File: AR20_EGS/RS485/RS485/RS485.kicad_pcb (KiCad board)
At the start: 2 copper layers, 12 x 15 mm, 6 parts, among them J1 Conn_01x06_Female, J2 Conn_01x02_Female, U1 MAX3362EKA+T

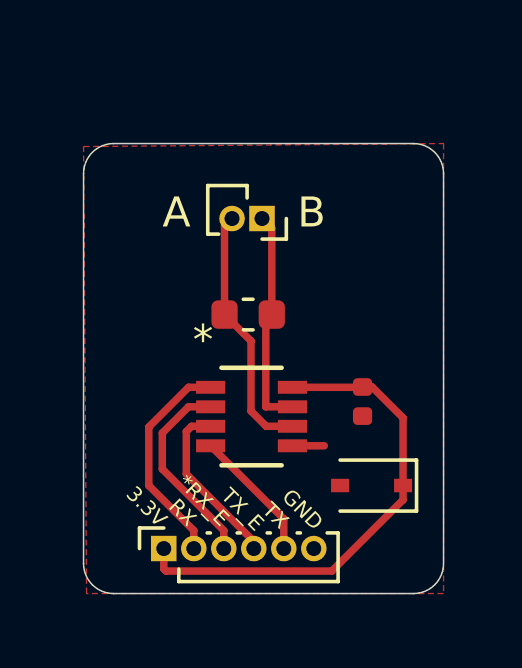
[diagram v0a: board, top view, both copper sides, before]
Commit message: Reverse polarity protection
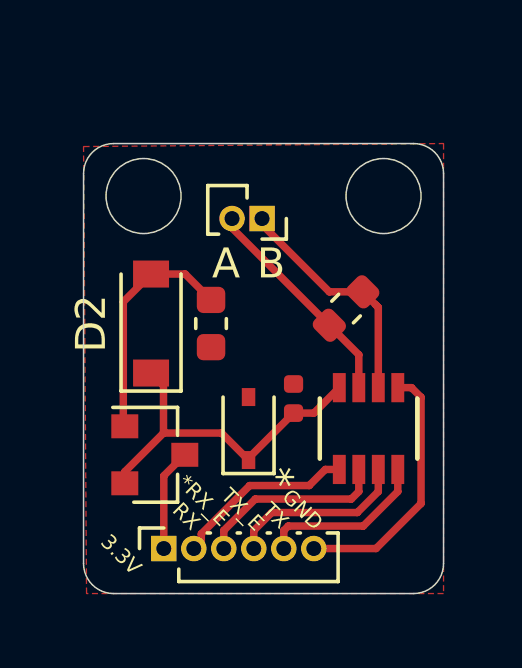
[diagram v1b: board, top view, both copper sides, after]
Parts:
- added D2: MBR0520LT, Diode_SMD:D_SOD-123, F.Cu at (150.2, 86.0)
- added Q1: PMOS_SQ2309ES-T1_GE3, RS485:PMOS_SQ2309ES, F.Cu at (150.4, 90.4)
- added R2: R10kΩ, RS485:C_0603_1608Metric, F.Cu at (152.2, 86.0)
- moved D1 4.52 mm to (153.5, 89.5), turned to 90 degrees
- moved U1 3.92 mm to (157.5, 89.5), turned to 90 degrees
- moved R1 3.27 mm to (156.8, 85.5), turned to 45 degrees
- moved C1 2.30 mm to (155.0, 88.5), turned to 270 degrees
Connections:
- C1 pad 2: +3V3 -> 3.3_filtered
- D1 pad 1: +3V3 -> 3.3_filtered
- J2 pad 1: /B -> /A
- J2 pad 2: /A -> /B
- U1 pad 8: +3V3 -> 3.3_filtered
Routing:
- net +3V3: track 16.4 -> 3.41 mm
- net 3.3_filtered: track 0.00 -> 11.7 mm
- net Net-(D2-Pad2): track 0.00 -> 7.84 mm
- net GND: track 1.06 -> 8.65 mm
- net TX: track 4.43 -> 5.68 mm
- net RX: track 7.28 -> 6.08 mm
- net /A: track 8.48 -> 7.89 mm
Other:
- outline, holes or cut-outs redrawn

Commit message: Silkscreen update
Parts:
- added G***: LOGO, RS485:AlignLogo, F.Cu at (158.2, 93.2)

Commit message: Added awesome, and Generated Gerber
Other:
- board text added: "3.3V-5V"
- board text removed: "3.3V"

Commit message: Fixed a little issue, New gerber files
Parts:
- added REF**: MountingHole_2.5mm, MountingHole:MountingHole_2.5mm, F.Cu at (150.0, 81.8)
- added REF**: MountingHole_2.5mm, MountingHole:MountingHole_2.5mm, F.Cu at (158.0, 81.8)
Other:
- outline, holes or cut-outs redrawn
